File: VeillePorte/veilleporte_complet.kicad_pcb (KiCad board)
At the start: 4 copper layers, 62.6 x 72.6 mm, 47 parts, among them J10 P-MFC, J19 Conn_01x02_Socket, J21 UART2 / RUI3, J22 SWD, J23 CABLE MODULE VL53L4CD, J3 Conn_01x02_Pin, J4 Conn_01x02_Pin, SW1 RESET, U1 RAK3172(H) / EU868, U2 BQ25570

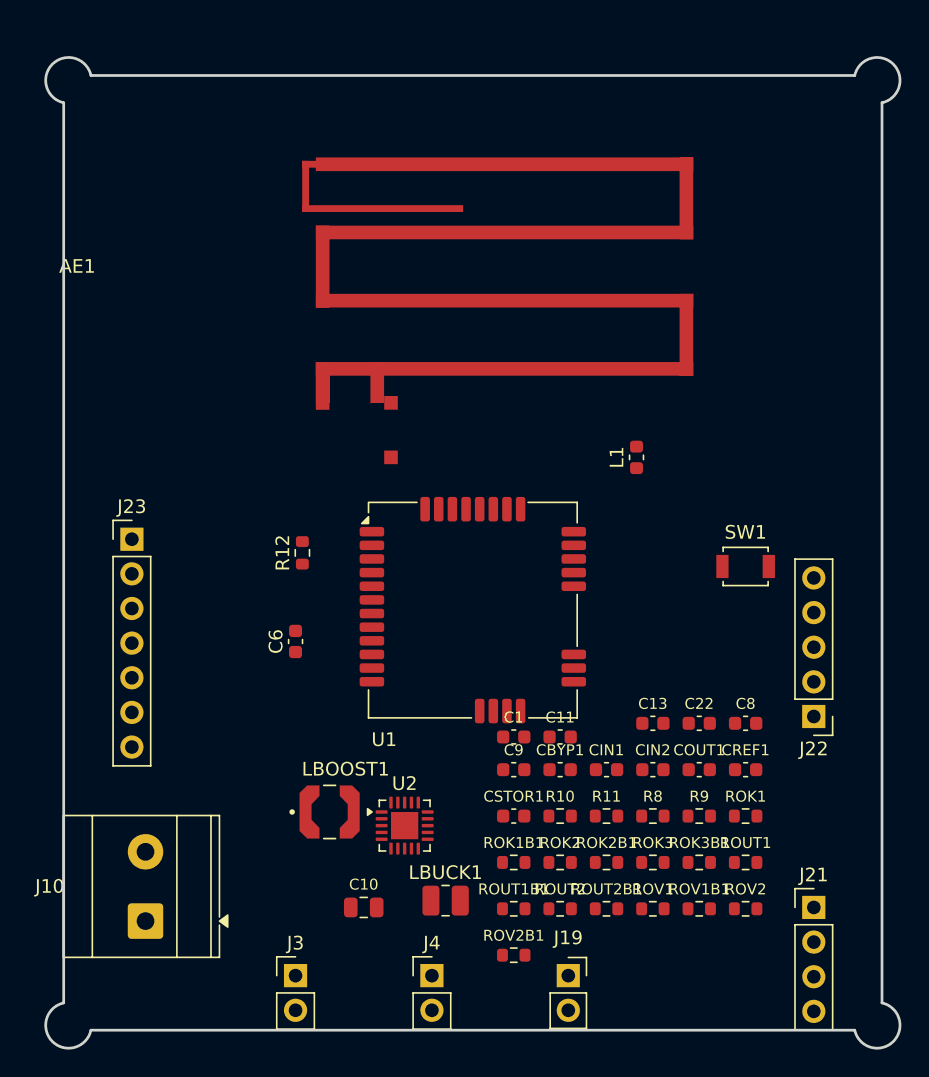
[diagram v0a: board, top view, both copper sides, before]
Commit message: Redimensionne le PCB VeillePorte en 40x60 mm
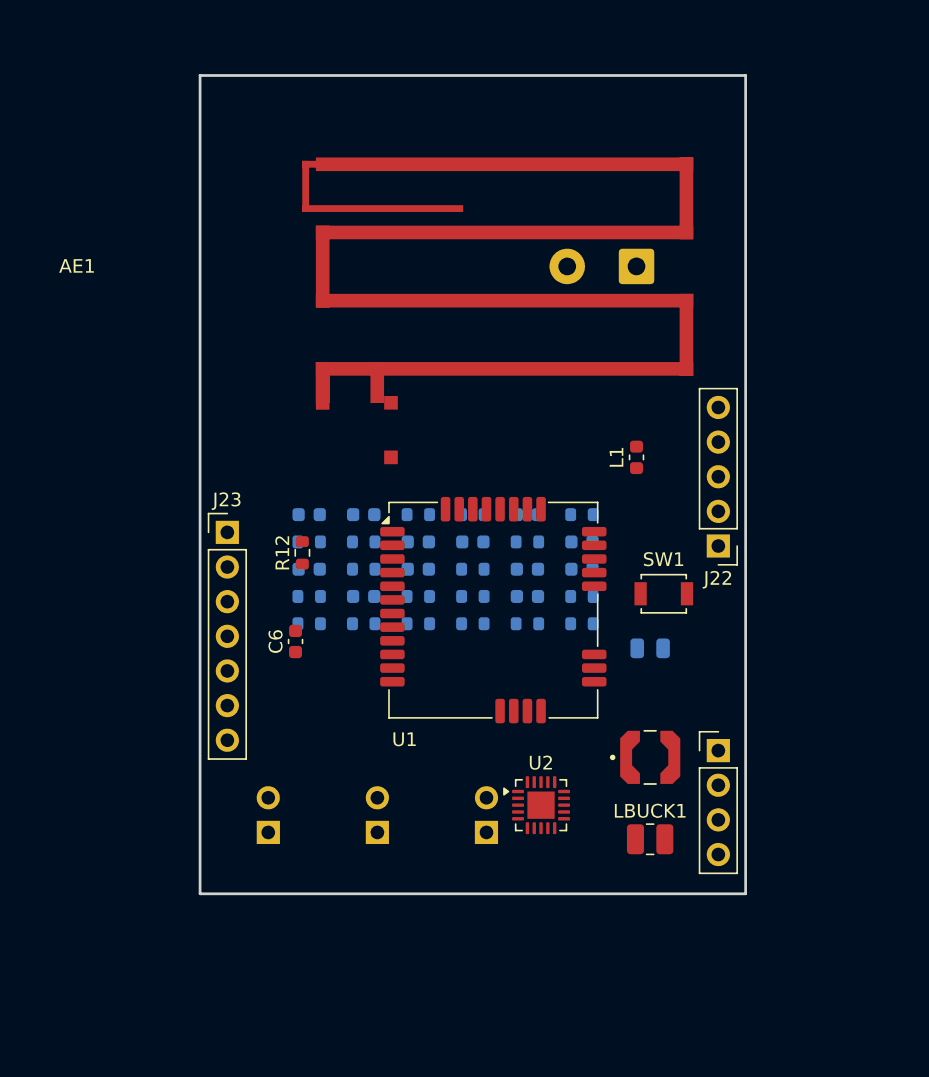
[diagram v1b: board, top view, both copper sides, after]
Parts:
- C1, C10, C11, C13, C22, C8, C9, CBYP1, CIN1, CIN2, COUT1, CREF1, CSTOR1, J19, J3, J4, R10, R11, R8, R9, ROK1, ROK1B1, ROK2, ROK2B1, ROK3, ROK3B1, ROUT1, ROUT1B1, ROUT2, ROUT2B1, ROV1, ROV1B1, ROV2, ROV2B1: moved to B.Cu
- moved J10 60.0 mm to (168.0, 42.0), turned to 180 degrees
- moved ROV1B1 35.5 mm to (152.0, 60.2)
- moved ROV2B1 32.4 mm to (156.0, 60.2)
- moved ROK2B1 32.1 mm to (144.0, 62.2)
- moved ROV2 31.9 mm to (156.0, 64.2)
- moved C8 31.9 mm to (148.0, 60.2)
- moved ROUT2B1 31.6 mm to (144.0, 66.2)
- moved ROUT1 29.7 mm to (152.0, 68.2)
- moved C10 28.3 mm to (169.0, 70.0)
- moved CREF1 28.1 mm to (152.0, 64.2)
- moved R8 27.9 mm to (148.0, 64.2)
- moved ROK2 27.6 mm to (148.0, 62.2)
- moved ROK3 27.5 mm to (148.0, 68.2)
- moved ROK3B1 26.9 mm to (164.0, 60.2)
- moved C22 26.3 mm to (148.0, 66.2)
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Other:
- board size 62.6 x 72.6 mm -> 40 x 60 mm

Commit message: Route first VeillePorte PCB signals
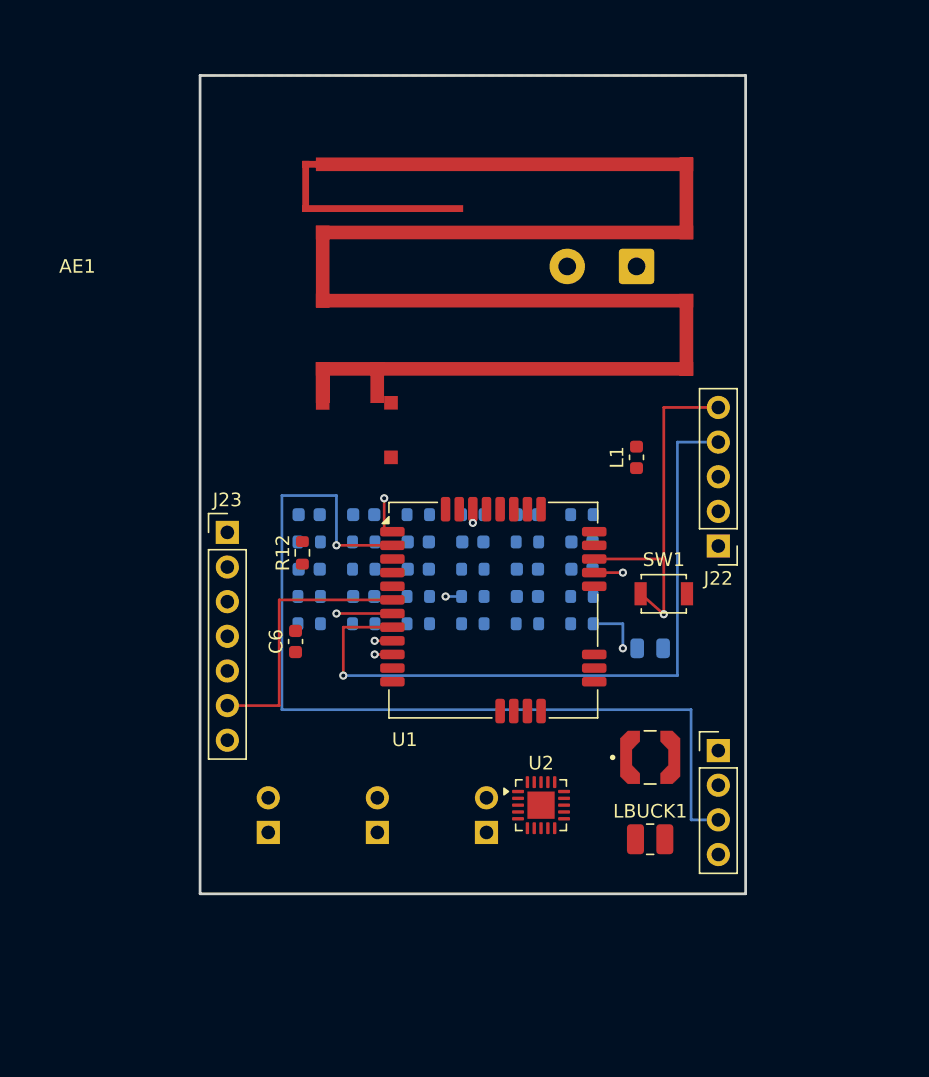
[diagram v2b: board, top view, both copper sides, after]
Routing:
- net /UART2_TX: track 0.00 -> 67.5 mm, vias 0 -> 1
- net IR_XSHUT: track 0.00 -> 54.9 mm, vias 0 -> 1
- net /UART2_RX: track 0.00 -> 53.7 mm, vias 0 -> 1
- net /SWCLK: track 0.00 -> 51.8 mm, vias 0 -> 1
- net /SWDIO: track 0.00 -> 42.1 mm, vias 0 -> 1
- net /NRST: track 0.00 -> 34.4 mm, vias 0 -> 2
- net IR_INT: track 0.00 -> 19.8 mm
- net /BOOT0: track 0.00 -> 16.4 mm, vias 0 -> 2
- net I2C_SDA: track 0.00 -> 16.0 mm, vias 0 -> 1
- net I2C_SCL: track 0.00 -> 12.4 mm, vias 0 -> 1
- added copper zone on B.Cu, net GND
- added copper zone on F.Cu, net GND
- added copper zone on In1.Cu, net GND
- added copper zone on B.Cu, net PWR
- added copper zone on F.Cu, net PWR
- added copper zone on In2.Cu, net PWR

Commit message: Reprendre implantation PCB quatre couches avant routage
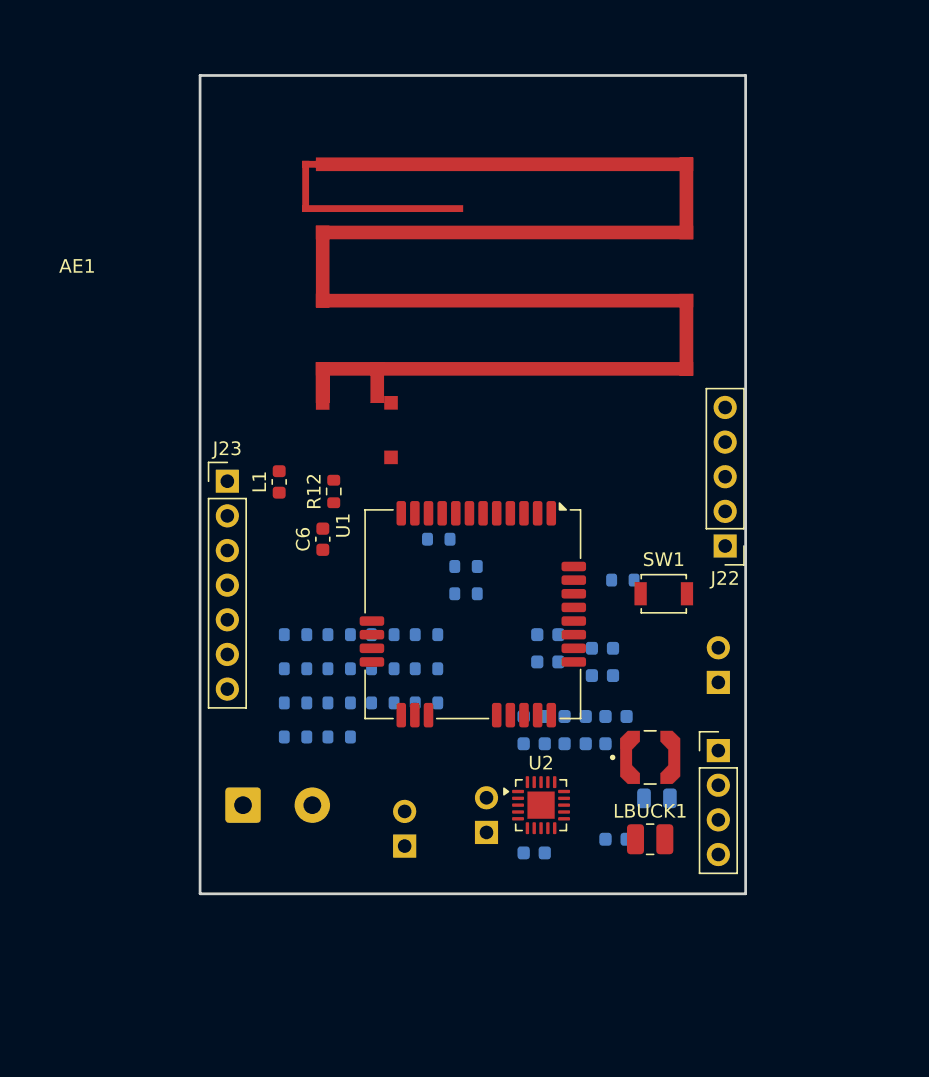
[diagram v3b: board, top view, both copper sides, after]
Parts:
- moved J10 48.9 mm to (139.2, 81.5), turned to 0 degrees
- moved J3 34.8 mm to (174.0, 72.5)
- moved L1 26.3 mm to (141.8, 57.8)
- moved C1 23.5 mm to (160.5, 77.0)
- moved C9 22.9 mm to (165.5, 72.0)
- moved ROK3B1 22.5 mm to (146.2, 74.0)
- moved CREF1 22.5 mm to (160.5, 85.0)
- moved ROV1 21.2 mm to (143.0, 69.0)
- moved C8 20.1 mm to (165.5, 70.0)
- moved COUT1 20.0 mm to (166.5, 84.0)
- moved ROK1 19.4 mm to (143.0, 71.5)
- moved CIN1 19.3 mm to (166.5, 75.0)
- moved CIN2 18.0 mm to (166.5, 77.0)
- moved C22 15.3 mm to (160.5, 75.0)
- moved ROUT1B1 13.7 mm to (143.0, 76.5)
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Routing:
- net /UART2_TX: track 67.5 -> 0.00 mm, vias 1 -> 0
- net IR_XSHUT: track 54.9 -> 0.00 mm, vias 1 -> 0
- net /UART2_RX: track 53.7 -> 0.00 mm, vias 1 -> 0
- net /SWCLK: track 51.8 -> 0.00 mm, vias 1 -> 0
- net /SWDIO: track 42.1 -> 0.00 mm, vias 1 -> 0
- net /NRST: track 34.4 -> 0.00 mm, vias 2 -> 0
- net IR_INT: track 19.8 -> 0.00 mm
- net /BOOT0: track 16.4 -> 0.00 mm, vias 2 -> 0
- net I2C_SDA: track 16.0 -> 0.00 mm, vias 1 -> 0
- net I2C_SCL: track 12.4 -> 0.00 mm, vias 1 -> 0
- removed copper zone on B.Cu, net GND
- removed copper zone on F.Cu, net GND
- removed copper zone on B.Cu, net PWR
- removed copper zone on F.Cu, net PWR
- removed copper zone on In2.Cu, net PWR

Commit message: Router VeillePorte en quatre couches avec GND In2 et exports 3D
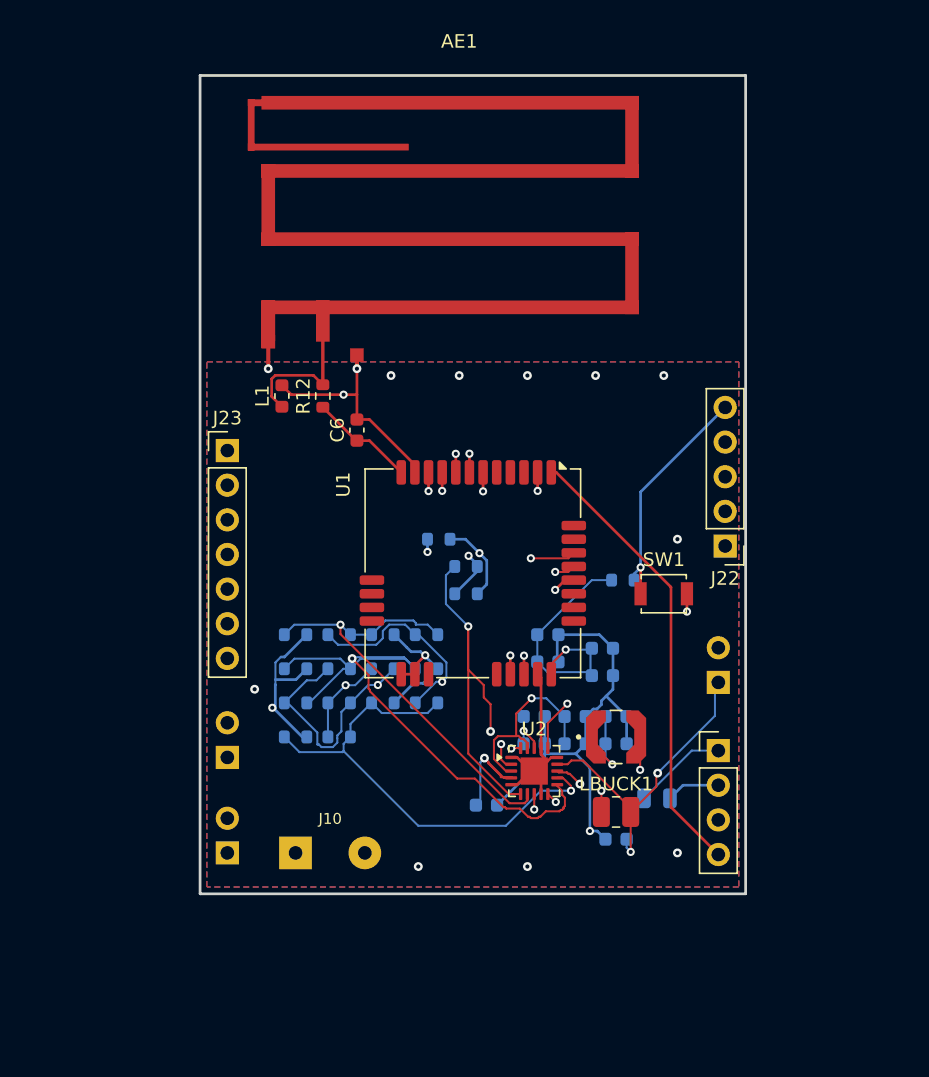
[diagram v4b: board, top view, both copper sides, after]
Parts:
- C6: footprint C_0603_1608Metric -> Capacitor_SMD:C_0603_1608Metric
- J10: value P-MFC -> PANNEAU SOLAIRE; footprint TerminalBlock_Phoenix:TerminalBlock_Phoenix_MKDS-3-2-5.08_1x02_P5.08mm_Horizontal -> VeillePorte_Connecteurs:Solar_Wires_2x_D1.0_P5.08
- J22: footprint Connector_PinHeader_2.54mm:PinHeader_1x05_P2.54mm_Vertical -> VeillePorte_Connecteurs:SWD_1x05_P2.54_VeillePorte
- L1: footprint L_0603_1608Metric -> Inductor_SMD:L_0603_1608Metric
- R12: footprint R_0603_1608Metric -> Resistor_SMD:R_0603_1608Metric
- U1: footprint RF_Module:RAK3172 -> VeillePorte_Modules:RAK3172_VeillePorte
- U2: footprint Package_DFN_QFN:QFN-20-1EP_3.5x3.5mm_P0.5mm_EP2x2mm -> VeillePorte_Modules:BQ25570_VeillePorte
- moved J19 19.1 mm to (138.0, 85.0)
- moved J4 14.5 mm to (138.0, 78.0)
- moved C6 8.38 mm to (147.5, 54.0)
- moved R12 7.05 mm to (145.0, 51.5)
- moved L1 6.30 mm to (142.0, 51.5)
- moved AE1 6.02 mm to (145.0, 47.5), turned to 0 degrees
- moved J10 5.20 mm to (143.0, 85.0)
- moved CREF1 4.95 mm to (157.0, 81.5)
- moved LBUCK1 3.20 mm to (166.5, 82.0)
- moved U1 3.00 mm to (156.0, 64.5)
- moved LBOOST1 2.92 mm to (166.5, 76.5)
- moved U2 2.55 mm to (160.5, 79.0)
- moved J23 2.25 mm to (138.0, 55.5)
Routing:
- net GND: track 0.00 -> 108.4 mm, vias 0 -> 19
- net PWR: track 0.00 -> 93.1 mm, vias 0 -> 1
- net /VRDIV: track 0.00 -> 48.2 mm, vias 0 -> 3
- net Net-(J19-Pin_2): track 0.00 -> 48.1 mm, vias 0 -> 1
- net Net-(U2-OK_PROG): track 0.00 -> 43.4 mm, vias 0 -> 1
- net Net-(J4-Pin_2): track 0.00 -> 41.5 mm, vias 0 -> 2
- net VBAT_OK: track 0.00 -> 38.9 mm, vias 0 -> 3
- net /UART2_TX: track 0.00 -> 38.7 mm, vias 0 -> 1
- net Net-(U2-VOUT_SET): track 0.00 -> 36.3 mm, vias 0 -> 1
- net Net-(U2-OK_HYST): track 0.00 -> 35.1 mm, vias 0 -> 2
- net /UART2_RX: track 0.00 -> 33.3 mm
- net Net-(U2-VBAT_OV): track 0.00 -> 32.9 mm, vias 0 -> 1
- net /NRST: track 0.00 -> 29.9 mm, vias 0 -> 2
- net IR_XSHUT: track 0.00 -> 29.4 mm, vias 0 -> 1
- net /SWDIO: track 0.00 -> 24.7 mm, vias 0 -> 1
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- added copper zone on B.Cu, net GND
- added copper zone on F.Cu, net GND
- added copper zone on In2.Cu, net GND
- removed copper zone on In1.Cu, net GND
